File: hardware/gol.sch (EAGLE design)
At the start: 74 parts, among them J1 TC2050-IDC, J2 2057-MCR-B-S-RA-TSMT-NP-CS4-T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, U1 STM32F072CBT, U2 AP2111H-3.3TRG1SOT-223_DIO-M

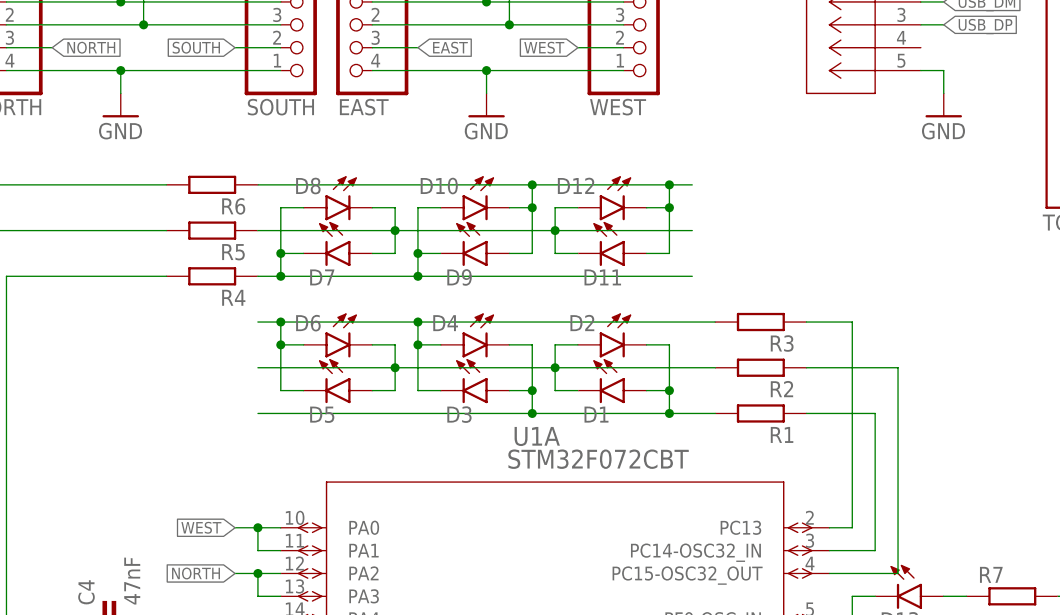
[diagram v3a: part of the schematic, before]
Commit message: removes R1..R3 from one of the charlieplexing ranges.
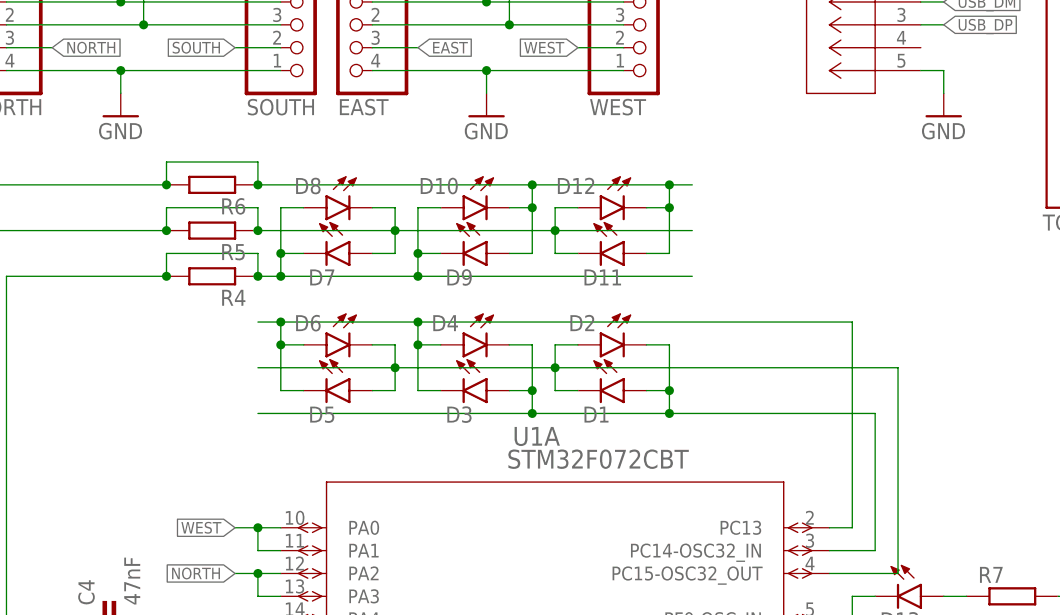
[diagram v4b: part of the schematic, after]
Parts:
- removed R1, R2, R3: R-EU-0207/8, parts:R-EU-0207/8
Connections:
- removed net N$13: D10.A, D7.C, D8.A, D9.C, R4.1
- removed net N$14: D11.C, D12.A, D7.A, D8.C, R5.1
- removed net N$15: D10.C, D11.A, D12.C, D9.A, R6.1
- removed net N$4: D1.A, D2.C, D3.A, D4.C, R1.2
- removed net N$5: D1.C, D2.A, D5.A, D6.C, R2.2
- removed net N$6: D3.C, D4.A, D5.C, D6.A, R3.2
- net OUTA-L1: now also D3.C, D4.A, D5.C, D6.A; no longer R3.1
- net OUTA-L2: now also D1.A, D2.C, D3.A, D4.C; no longer R1.1
- net OUTA-L3: now also D1.C, D2.A, D5.A, D6.C; no longer R2.1
- net OUTB-L1: now also D10.A, D7.C, D8.A, D9.C, R4.1
- net OUTB-L2: now also D11.C, D12.A, D7.A, D8.C, R5.1
- net OUTB-L3: now also D10.C, D11.A, D12.C, D9.A, R6.1
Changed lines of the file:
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@@
 <part name="SUPPLY2" library="supply2" library_urn="urn:adsk.eagle:library:372" deviceset="V+" device=""/>
 <part name="GND2" library="supply1" library_urn="urn:adsk.eagle:library:371" deviceset="GND" device=""/>
-<part name="R1" library="parts" deviceset="R-EU-0207/8" device=""/>
-<part name="R2" library="parts" deviceset="R-EU-0207/8" device=""/>
-<part name="R3" library="parts" deviceset="R-EU-0207/8" device=""/>
 <part name="R4" library="parts" deviceset="R-EU-0207/8" device=""/>
 <part name="R5" library="parts" deviceset="R-EU-0207/8" device=""/>
@@
 <attribute name="VALUE" x="226.06" y="137.16" size="1.778" layer="96"/>
 </instance>
-<instance part="R1" gate="G$1" x="99.06" y="114.3" smashed="yes" rot="R180">
-<attribute name="NAME" x="102.87" y="112.8014" size="1.778" layer="95" rot="R180"/>
-</instance>
-<instance part="R2" gate="G$1" x="99.06" y="119.38" smashed="yes" rot="R180">
-<attribute name="NAME" x="102.87" y="117.8814" size="1.778" layer="95" rot="R180"/>
-</instance>
-<instance part="R3" gate="G$1" x="99.06" y="124.46" smashed="yes" rot="R180">
-<attribute name="NAME" x="102.87" y="122.9614" size="1.778" layer="95" rot="R180"/>
-</instance>
 <instance part="R4" gate="G$1" x="38.1" y="129.54" smashed="yes" rot="R180">
 <attribute name="NAME" x="41.91" y="128.0414" size="1.778" layer="95" rot="R180"/>
@@
 </segment>
 </net>
-<net name="N$4" class="0">
-<segment>
-<pinref part="R1" gate="G$1" pin="2"/>
-<wire x1="93.98" y1="114.3" x2="88.9" y2="114.3" width="0.1524" layer="91"/>
+<net name="OUTA-L2" class="0">
+<segment>
+<pinref part="U1" gate="A" pin="PC14-OSC32_IN"/>
+<wire x1="111.76" y1="114.3" x2="111.76" y2="99.06" width="0.1524" layer="91"/>
+<wire x1="111.76" y1="99.06" x2="106.68" y2="99.06" width="0.1524" layer="91"/>
 <pinref part="D1" gate="G$1" pin="A"/>
 <wire x1="88.9" y1="114.3" x2="73.66" y2="114.3" width="0.1524" layer="91"/>
@@
 <wire x1="73.66" y1="121.92" x2="73.66" y2="116.84" width="0.1524" layer="91"/>
 <junction x="73.66" y="116.84"/>
-</segment>
-</net>
-<net name="N$5" class="0">
-<segment>
-<pinref part="R2" gate="G$1" pin="2"/>
-<wire x1="93.98" y1="119.38" x2="76.2" y2="119.38" width="0.1524" layer="91"/>
+<wire x1="88.9" y1="114.3" x2="111.76" y2="114.3" width="0.1524" layer="91"/>
+</segment>
+</net>
+<net name="OUTA-L3" class="0">
+<segment>
+<pinref part="U1" gate="A" pin="PC15-OSC32_OUT"/>
+<wire x1="106.68" y1="96.52" x2="114.3" y2="96.52" width="0.1524" layer="91"/>
+<wire x1="114.3" y1="96.52" x2="114.3" y2="119.38" width="0.1524" layer="91"/>
+<wire x1="114.3" y1="119.38" x2="76.2" y2="119.38" width="0.1524" layer="91"/>
 <pinref part="D1" gate="G$1" pin="C"/>
 <wire x1="76.2" y1="119.38" x2="58.42" y2="119.38" width="0.1524" layer="91"/>
@@
 </segment>
 </net>
-<net name="N$6" class="0">
-<segment>
-<pinref part="R3" gate="G$1" pin="2"/>
-<wire x1="93.98" y1="124.46" x2="60.96" y2="124.46" width="0.1524" layer="91"/>
+<net name="OUTA-L1" class="0">
+<segment>
+<pinref part="U1" gate="A" pin="PC13"/>
+<wire x1="106.68" y1="101.6" x2="109.22" y2="101.6" width="0.1524" layer="91"/>
+<wire x1="109.22" y1="101.6" x2="109.22" y2="124.46" width="0.1524" layer="91"/>
 <pinref part="D3" gate="G$1" pin="C"/>
+<wire x1="109.22" y1="124.46" x2="60.96" y2="124.46" width="0.1524" layer="91"/>
 <wire x1="60.96" y1="124.46" x2="45.72" y2="124.46" width="0.1524" layer="91"/>
 <wire x1="45.72" y1="124.46" x2="43.18" y2="124.46" width="0.1524" layer="91"/>
@@
 </segment>
 </net>
-<net name="OUTA-L2" class="0">
-<segment>
-<pinref part="U1" gate="A" pin="PC14-OSC32_IN"/>
-<wire x1="111.76" y1="114.3" x2="111.76" y2="99.06" width="0.1524" layer="91"/>
-<wire x1="111.76" y1="99.06" x2="106.68" y2="99.06" width="0.1524" layer="91"/>
-<pinref part="R1" gate="G$1" pin="1"/>
-<wire x1="111.76" y1="114.3" x2="104.14" y2="114.3" width="0.1524" layer="91"/>
-</segment>
-</net>
-<net name="OUTA-L3" class="0">
-<segment>
-<pinref part="U1" gate="A" pin="PC15-OSC32_OUT"/>
-<wire x1="106.68" y1="96.52" x2="114.3" y2="96.52" width="0.1524" layer="91"/>
-<wire x1="114.3" y1="96.52" x2="114.3" y2="119.38" width="0.1524" layer="91"/>
-<pinref part="R2" gate="G$1" pin="1"/>
-<wire x1="114.3" y1="119.38" x2="104.14" y2="119.38" width="0.1524" layer="91"/>
-</segment>
-</net>
-<net name="OUTA-L1" class="0">
-<segment>
-<pinref part="U1" gate="A" pin="PC13"/>
-<wire x1="106.68" y1="101.6" x2="109.22" y2="101.6" width="0.1524" layer="91"/>
-<wire x1="109.22" y1="101.6" x2="109.22" y2="124.46" width="0.1524" layer="91"/>
-<pinref part="R3" gate="G$1" pin="1"/>
-<wire x1="109.22" y1="124.46" x2="104.14" y2="124.46" width="0.1524" layer="91"/>
-</segment>
-</net>
 <net name="OUTB-L1" class="0">
 <segment>
@@
 <pinref part="U1" gate="A" pin="PA15"/>
 <wire x1="15.24" y1="63.5" x2="45.72" y2="63.5" width="0.1524" layer="91"/>
-</segment>
-</net>
-<net name="OUTB-L2" class="0">
-<segment>
-<pinref part="R5" gate="G$1" pin="2"/>
-<wire x1="12.7" y1="30.48" x2="12.7" y2="134.62" width="0.1524" layer="91"/>
-<wire x1="12.7" y1="134.62" x2="33.02" y2="134.62" width="0.1524" layer="91"/>
-<wire x1="12.7" y1="30.48" x2="38.1" y2="30.48" width="0.1524" layer="91"/>
-<pinref part="U1" gate="A" pin="PB12"/>
-<wire x1="38.1" y1="30.48" x2="38.1" y2="27.94" width="0.1524" layer="91"/>
-<wire x1="38.1" y1="27.94" x2="45.72" y2="27.94" width="0.1524" layer="91"/>
-</segment>
-</net>
-<net name="OUTB-L3" class="0">
-<segment>
-<pinref part="R6" gate="G$1" pin="2"/>
-<wire x1="10.16" y1="81.28" x2="10.16" y2="139.7" width="0.1524" layer="91"/>
-<wire x1="10.16" y1="139.7" x2="33.02" y2="139.7" width="0.1524" layer="91"/>
-<pinref part="U1" gate="A" pin="PA8"/>
-<wire x1="45.72" y1="81.28" x2="10.16" y2="81.28" width="0.1524" layer="91"/>
-</segment>
-</net>
-<net name="N$13" class="0">
-<segment>
 <pinref part="R4" gate="G$1" pin="1"/>
 <wire x1="43.18" y1="129.54" x2="45.72" y2="129.54" width="0.1524" layer="91"/>
@@
 <junction x="60.96" y="129.54"/>
 <junction x="60.96" y="132.08"/>
-</segment>
-</net>
-<net name="N$14" class="0">
-<segment>
+<wire x1="43.18" y1="129.54" x2="43.18" y2="132.08" width="0.1524" layer="91"/>
+<junction x="43.18" y="129.54"/>
+<wire x1="43.18" y1="132.08" x2="33.02" y2="132.08" width="0.1524" layer="91"/>
+<wire x1="33.02" y1="132.08" x2="33.02" y2="129.54" width="0.1524" layer="91"/>
+<junction x="33.02" y="129.54"/>
+</segment>
+</net>
+<net name="OUTB-L2" class="0">
+<segment>
+<pinref part="R5" gate="G$1" pin="2"/>
+<wire x1="12.7" y1="30.48" x2="12.7" y2="134.62" width="0.1524" layer="91"/>
+<wire x1="12.7" y1="134.62" x2="33.02" y2="134.62" width="0.1524" layer="91"/>
+<wire x1="12.7" y1="30.48" x2="38.1" y2="30.48" width="0.1524" layer="91"/>
+<pinref part="U1" gate="A" pin="PB12"/>
+<wire x1="38.1" y1="30.48" x2="38.1" y2="27.94" width="0.1524" layer="91"/>
+<wire x1="38.1" y1="27.94" x2="45.72" y2="27.94" width="0.1524" layer="91"/>
 <pinref part="R5" gate="G$1" pin="1"/>
 <wire x1="43.18" y1="134.62" x2="58.42" y2="134.62" width="0.1524" layer="91"/>
@@
 <wire x1="78.74" y1="137.16" x2="76.2" y2="137.16" width="0.1524" layer="91"/>
 <wire x1="76.2" y1="137.16" x2="76.2" y2="134.62" width="0.1524" layer="91"/>
-</segment>
-</net>
-<net name="N$15" class="0">
-<segment>
+<wire x1="43.18" y1="134.62" x2="43.18" y2="137.16" width="0.1524" layer="91"/>
+<junction x="43.18" y="134.62"/>
+<wire x1="43.18" y1="137.16" x2="33.02" y2="137.16" width="0.1524" layer="91"/>
+<wire x1="33.02" y1="137.16" x2="33.02" y2="134.62" width="0.1524" layer="91"/>
+<junction x="33.02" y="134.62"/>
+</segment>
+</net>
+<net name="OUTB-L3" class="0">
+<segment>
+<pinref part="R6" gate="G$1" pin="2"/>
+<wire x1="10.16" y1="81.28" x2="10.16" y2="139.7" width="0.1524" layer="91"/>
+<wire x1="10.16" y1="139.7" x2="33.02" y2="139.7" width="0.1524" layer="91"/>
+<pinref part="U1" gate="A" pin="PA8"/>
+<wire x1="45.72" y1="81.28" x2="10.16" y2="81.28" width="0.1524" layer="91"/>
 <pinref part="R6" gate="G$1" pin="1"/>
 <wire x1="43.18" y1="139.7" x2="73.66" y2="139.7" width="0.1524" layer="91"/>
@@
 <wire x1="86.36" y1="137.16" x2="88.9" y2="137.16" width="0.1524" layer="91"/>
 <junction x="88.9" y="137.16"/>
-</segment>
-</net>
+<wire x1="43.18" y1="139.7" x2="43.18" y2="142.24" width="0.1524" layer="91"/>
+<junction x="43.18" y="139.7"/>
+<wire x1="43.18" y1="142.24" x2="33.02" y2="142.24" width="0.1524" layer="91"/>
+<wire x1="33.02" y1="142.24" x2="33.02" y2="139.7" width="0.1524" layer="91"/>
+<junction x="33.02" y="139.7"/>
+</segment>
+</net>

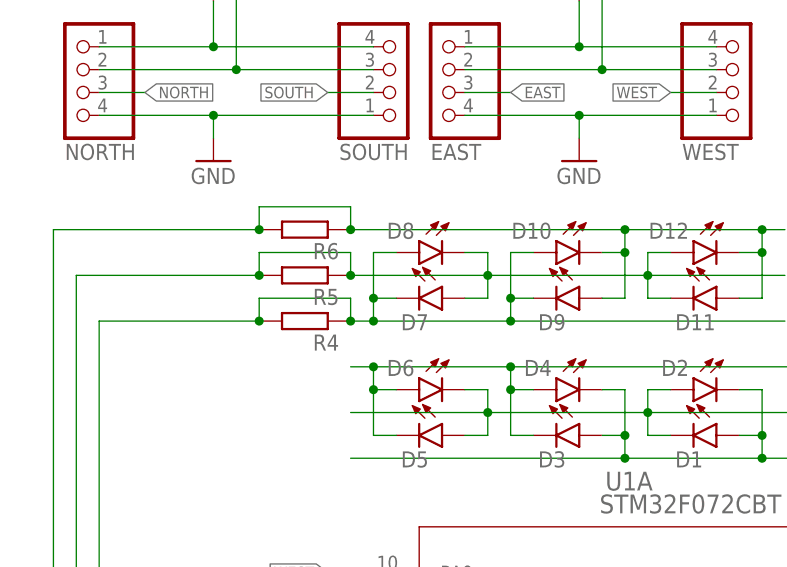
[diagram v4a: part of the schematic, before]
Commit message: Removes R4-R6 for charlieplexing B.
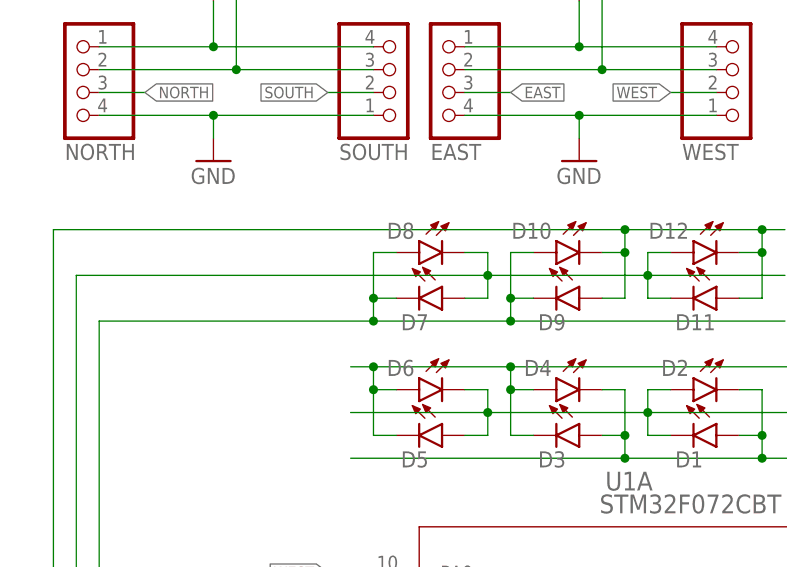
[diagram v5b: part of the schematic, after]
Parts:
- removed R4, R5, R6: R-EU-0207/8, parts:R-EU-0207/8
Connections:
- net OUTB-L1: no longer R4.1, R4.2
- net OUTB-L2: no longer R5.1, R5.2
- net OUTB-L3: no longer R6.1, R6.2
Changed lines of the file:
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@@
 <part name="SUPPLY2" library="supply2" library_urn="urn:adsk.eagle:library:372" deviceset="V+" device=""/>
 <part name="GND2" library="supply1" library_urn="urn:adsk.eagle:library:371" deviceset="GND" device=""/>
-<part name="R4" library="parts" deviceset="R-EU-0207/8" device=""/>
-<part name="R5" library="parts" deviceset="R-EU-0207/8" device=""/>
-<part name="R6" library="parts" deviceset="R-EU-0207/8" device=""/>
 <part name="R7" library="parts" deviceset="R-EU-0207/8" device=""/>
 <part name="R8" library="parts" deviceset="R-EU-0207/8" device=""/>
@@
 <attribute name="VALUE" x="226.06" y="137.16" size="1.778" layer="96"/>
 </instance>
-<instance part="R4" gate="G$1" x="38.1" y="129.54" smashed="yes" rot="R180">
-<attribute name="NAME" x="41.91" y="128.0414" size="1.778" layer="95" rot="R180"/>
-</instance>
-<instance part="R5" gate="G$1" x="38.1" y="134.62" smashed="yes" rot="R180">
-<attribute name="NAME" x="41.91" y="133.1214" size="1.778" layer="95" rot="R180"/>
-</instance>
-<instance part="R6" gate="G$1" x="38.1" y="139.7" smashed="yes" rot="R180">
-<attribute name="NAME" x="41.91" y="138.2014" size="1.778" layer="95" rot="R180"/>
-</instance>
 <instance part="R7" gate="G$1" x="127" y="93.98" smashed="yes">
 <attribute name="NAME" x="123.19" y="95.4786" size="1.778" layer="95"/>
@@
 <net name="OUTB-L1" class="0">
 <segment>
-<pinref part="R4" gate="G$1" pin="2"/>
 <wire x1="15.24" y1="63.5" x2="15.24" y2="129.54" width="0.1524" layer="91"/>
-<wire x1="15.24" y1="129.54" x2="33.02" y2="129.54" width="0.1524" layer="91"/>
+<wire x1="15.24" y1="129.54" x2="45.72" y2="129.54" width="0.1524" layer="91"/>
 <pinref part="U1" gate="A" pin="PA15"/>
 <wire x1="15.24" y1="63.5" x2="45.72" y2="63.5" width="0.1524" layer="91"/>
-<pinref part="R4" gate="G$1" pin="1"/>
-<wire x1="43.18" y1="129.54" x2="45.72" y2="129.54" width="0.1524" layer="91"/>
 <pinref part="D7" gate="G$1" pin="C"/>
 <wire x1="45.72" y1="129.54" x2="60.96" y2="129.54" width="0.1524" layer="91"/>
@@
 <junction x="60.96" y="129.54"/>
 <junction x="60.96" y="132.08"/>
-<wire x1="43.18" y1="129.54" x2="43.18" y2="132.08" width="0.1524" layer="91"/>
-<junction x="43.18" y="129.54"/>
-<wire x1="43.18" y1="132.08" x2="33.02" y2="132.08" width="0.1524" layer="91"/>
-<wire x1="33.02" y1="132.08" x2="33.02" y2="129.54" width="0.1524" layer="91"/>
-<junction x="33.02" y="129.54"/>
 </segment>
 </net>
 <net name="OUTB-L2" class="0">
 <segment>
-<pinref part="R5" gate="G$1" pin="2"/>
 <wire x1="12.7" y1="30.48" x2="12.7" y2="134.62" width="0.1524" layer="91"/>
-<wire x1="12.7" y1="134.62" x2="33.02" y2="134.62" width="0.1524" layer="91"/>
+<wire x1="12.7" y1="134.62" x2="58.42" y2="134.62" width="0.1524" layer="91"/>
 <wire x1="12.7" y1="30.48" x2="38.1" y2="30.48" width="0.1524" layer="91"/>
 <pinref part="U1" gate="A" pin="PB12"/>
 <wire x1="38.1" y1="30.48" x2="38.1" y2="27.94" width="0.1524" layer="91"/>
 <wire x1="38.1" y1="27.94" x2="45.72" y2="27.94" width="0.1524" layer="91"/>
-<pinref part="R5" gate="G$1" pin="1"/>
-<wire x1="43.18" y1="134.62" x2="58.42" y2="134.62" width="0.1524" layer="91"/>
 <pinref part="D7" gate="G$1" pin="A"/>
 <wire x1="58.42" y1="134.62" x2="76.2" y2="134.62" width="0.1524" layer="91"/>
@@
 <wire x1="78.74" y1="137.16" x2="76.2" y2="137.16" width="0.1524" layer="91"/>
 <wire x1="76.2" y1="137.16" x2="76.2" y2="134.62" width="0.1524" layer="91"/>
-<wire x1="43.18" y1="134.62" x2="43.18" y2="137.16" width="0.1524" layer="91"/>
-<junction x="43.18" y="134.62"/>
-<wire x1="43.18" y1="137.16" x2="33.02" y2="137.16" width="0.1524" layer="91"/>
-<wire x1="33.02" y1="137.16" x2="33.02" y2="134.62" width="0.1524" layer="91"/>
-<junction x="33.02" y="134.62"/>
 </segment>
 </net>
 <net name="OUTB-L3" class="0">
 <segment>
-<pinref part="R6" gate="G$1" pin="2"/>
 <wire x1="10.16" y1="81.28" x2="10.16" y2="139.7" width="0.1524" layer="91"/>
-<wire x1="10.16" y1="139.7" x2="33.02" y2="139.7" width="0.1524" layer="91"/>
+<wire x1="10.16" y1="139.7" x2="73.66" y2="139.7" width="0.1524" layer="91"/>
 <pinref part="U1" gate="A" pin="PA8"/>
 <wire x1="45.72" y1="81.28" x2="10.16" y2="81.28" width="0.1524" layer="91"/>
-<pinref part="R6" gate="G$1" pin="1"/>
-<wire x1="43.18" y1="139.7" x2="73.66" y2="139.7" width="0.1524" layer="91"/>
 <pinref part="D9" gate="G$1" pin="A"/>
 <wire x1="73.66" y1="139.7" x2="88.9" y2="139.7" width="0.1524" layer="91"/>
@@
 <wire x1="86.36" y1="137.16" x2="88.9" y2="137.16" width="0.1524" layer="91"/>
 <junction x="88.9" y="137.16"/>
-<wire x1="43.18" y1="139.7" x2="43.18" y2="142.24" width="0.1524" layer="91"/>
-<junction x="43.18" y="139.7"/>
-<wire x1="43.18" y1="142.24" x2="33.02" y2="142.24" width="0.1524" layer="91"/>
-<wire x1="33.02" y1="142.24" x2="33.02" y2="139.7" width="0.1524" layer="91"/>
-<junction x="33.02" y="139.7"/>
-</segment>
-</net>
+</segment>
+</net>
